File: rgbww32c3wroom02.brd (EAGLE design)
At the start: 36.8 x 20.3 mm, 25 parts

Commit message: small changes on the 12V side
moved the input caps so that the 12V pins are now oriented towards the switching controller. nothing major but might get a wee bit better filtering due to smaller loop area
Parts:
- moved C4 0.79 mm to (19.4, 77.6), turned to 90 degrees
- moved C3 0.16 mm to (22.1, 77.2), turned to 90 degrees
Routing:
- net 12V: track 11.6 -> 0.00 mm
- net GND: track 17.9 -> 17.2 mm
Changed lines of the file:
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@@
 <setting verticaltext="up"/>
 </settings>
-<grid distance="0.05" unitdist="inch" unit="inch" style="lines" multiple="1" display="no" altdistance="0.00625" altunitdist="inch" altunit="inch"/>
+<grid distance="0.05" unitdist="inch" unit="mm" style="lines" multiple="1" display="no" altdistance="0.00625" altunitdist="inch" altunit="mm"/>
 <layers>
 <layer number="1" name="Top" color="4" fill="1" visible="yes" active="yes"/>
@@
 Rev 23
 2023 Peter Jakobs</text>
+<text x="16.66875" y="72.86625" size="0.6096" layer="26" rot="MR90">ESP_RX</text>
 </plain>
 <attributes>
@@
 <element name="U$5" library="ESP32C3M" package="SMD" value="ESP32C3WROOM02" x="6.6675" y="69.85" rot="R90"/>
 <element name="U$6" library="TI_Components" package="SOT23-6" value="TPS5604030" x="20.32" y="70.485" rot="R180"/>
-<element name="C3" library="rcl" package="C1210" value="4.7µF" x="21.9075" y="77.1525" smashed="yes" rot="R270"/>
-<element name="C4" library="rcl" package="C0805" value="100nF" x="18.7325" y="77.1525" smashed="yes" rot="R270"/>
+<element name="C3" library="rcl" package="C1210" value="4.7µF" x="22.06625" y="77.1525" smashed="yes" rot="R90"/>
+<element name="C4" library="rcl" package="C0805" value="100nF" x="19.3675" y="77.62875" smashed="yes" rot="R90"/>
 <element name="R8" library="rcl" package="M0805" value="412kOhm" x="15.39875" y="77.31125" smashed="yes" rot="R90"/>
 <element name="R9" library="rcl" package="M0805" value="200kOhm" x="15.71625" y="77.31125" smashed="yes" rot="MR270">
@@
 <contactref element="C3" pad="2"/>
 <contactref element="C4" pad="2"/>
-<via x="18.7325" y="74.6125" extent="1-16" drill="0.6"/>
+<via x="17.4625" y="78.4225" extent="1-16" drill="0.6"/>
 <via x="22.225" y="71.755" extent="1-16" drill="0.6"/>
 <wire x1="20.57" y1="72.01" x2="21.97" y2="72.01" width="0.4064" layer="1"/>
 <wire x1="21.97" y1="72.01" x2="22.225" y2="71.755" width="0.4064" layer="1"/>
-<wire x1="18.7325" y1="74.6125" x2="18.7325" y2="76.2025" width="0.4064" layer="1"/>
-<wire x1="21.9075" y1="75.7525" x2="21.59" y2="74.93" width="0.4064" layer="1"/>
-<wire x1="21.59" y1="74.93" x2="21.2725" y2="74.6125" width="0.4064" layer="1"/>
-<wire x1="21.2725" y1="74.6125" x2="18.7325" y2="74.6125" width="0.4064" layer="1"/>
+<wire x1="17.4625" y1="78.4225" x2="19.21125" y2="78.4225" width="0.4064" layer="1"/>
+<wire x1="19.21125" y1="78.4225" x2="19.3675" y2="78.57875" width="0.4064" layer="1"/>
+<wire x1="19.3675" y1="78.57875" x2="22.04" y2="78.57875" width="0.4064" layer="1"/>
+<wire x1="22.04" y1="78.57875" x2="22.06625" y2="78.5525" width="0.4064" layer="1"/>
 </signal>
 <signal name="CH1">
@@
 <contactref element="SV1" pad="2"/>
 <polygon width="0.3048" layer="1">
-<vertex x="12.7" y="80.01"/>
+<vertex x="13.97" y="80.01"/>
 <vertex x="36.83" y="80.01"/>
 <vertex x="36.83" y="72.39"/>
@@
 <vertex x="23.1775" y="73.81875"/>
 <vertex x="23.1775" y="71.12"/>
-<vertex x="12.7" y="71.12"/>
+<vertex x="13.97" y="71.12"/>
 </polygon>
 <contactref element="U$6" pad="5"/>
@@
 <contactref element="C4" pad="1"/>
 <contactref element="C3" pad="1"/>
-<wire x1="22.0925" y1="78.42" x2="21.9075" y2="78.5525" width="0.4064" layer="1"/>
-<wire x1="18.32" y1="72.01" x2="19.305" y2="72.01" width="0.4064" layer="1"/>
-<wire x1="19.305" y1="72.01" x2="19.52625" y2="72.23125" width="0.4064" layer="1"/>
-<wire x1="19.52625" y1="72.23125" x2="19.52625" y2="73.50125" width="0.4064" layer="1"/>
-<wire x1="19.52625" y1="73.50125" x2="19.3675" y2="73.66" width="0.4064" layer="1"/>
-<wire x1="19.3675" y1="73.66" x2="17.30375" y2="73.66" width="0.4064" layer="1"/>
-<wire x1="17.30375" y1="73.66" x2="16.98625" y2="73.9775" width="0.4064" layer="1"/>
-<wire x1="16.98625" y1="73.9775" x2="16.98625" y2="78.105" width="0.4064" layer="1"/>
-<wire x1="16.98625" y1="78.105" x2="17.30375" y2="78.4225" width="0.4064" layer="1"/>
-<wire x1="17.30375" y1="78.4225" x2="18.25375" y2="78.4225" width="0.4064" layer="1"/>
-<wire x1="18.25375" y1="78.4225" x2="18.7325" y2="78.1025" width="0.4064" layer="1"/>
 </signal>
 <signal name="3V3">
@@
 <wire x1="12.7" y1="64.4525" x2="8.73125" y2="64.4525" width="0.3048" layer="1"/>
 <wire x1="23.1775" y1="63.97625" x2="23.1775" y2="65.0875" width="0.3048" layer="1"/>
-<wire x1="23.1775" y1="65.0875" x2="23.65375" y2="65.56375" width="0.3048" layer="1"/>
-<wire x1="23.65375" y1="65.56375" x2="24.60625" y2="65.56375" width="0.3048" layer="1"/>
-<wire x1="24.60625" y1="65.56375" x2="25.24125" y2="66.19875" width="0.3048" layer="1"/>
-<wire x1="25.24125" y1="66.19875" x2="25.24125" y2="67.0525" width="0.3048" layer="1"/>
+<wire x1="23.1775" y1="65.0875" x2="23.97125" y2="65.88125" width="0.3048" layer="1"/>
 <wire x1="25.24125" y1="67.0525" x2="25.34" y2="67.15125" width="0.3048" layer="1"/>
 <wire x1="13.6525" y1="63.5" x2="22.70125" y2="63.5" width="0.3048" layer="1"/>
 <wire x1="22.70125" y1="63.5" x2="23.1775" y2="63.97625" width="0.3048" layer="1"/>
+<wire x1="23.97125" y1="65.88125" x2="23.97125" y2="66.83375" width="0.3048" layer="1"/>
+<wire x1="25.24125" y1="67.0525" x2="24.19" y2="67.0525" width="0.3048" layer="1"/>
+<wire x1="24.19" y1="67.0525" x2="23.97125" y2="66.83375" width="0.3048" layer="1"/>
 </signal>
 <signal name="CH4S">

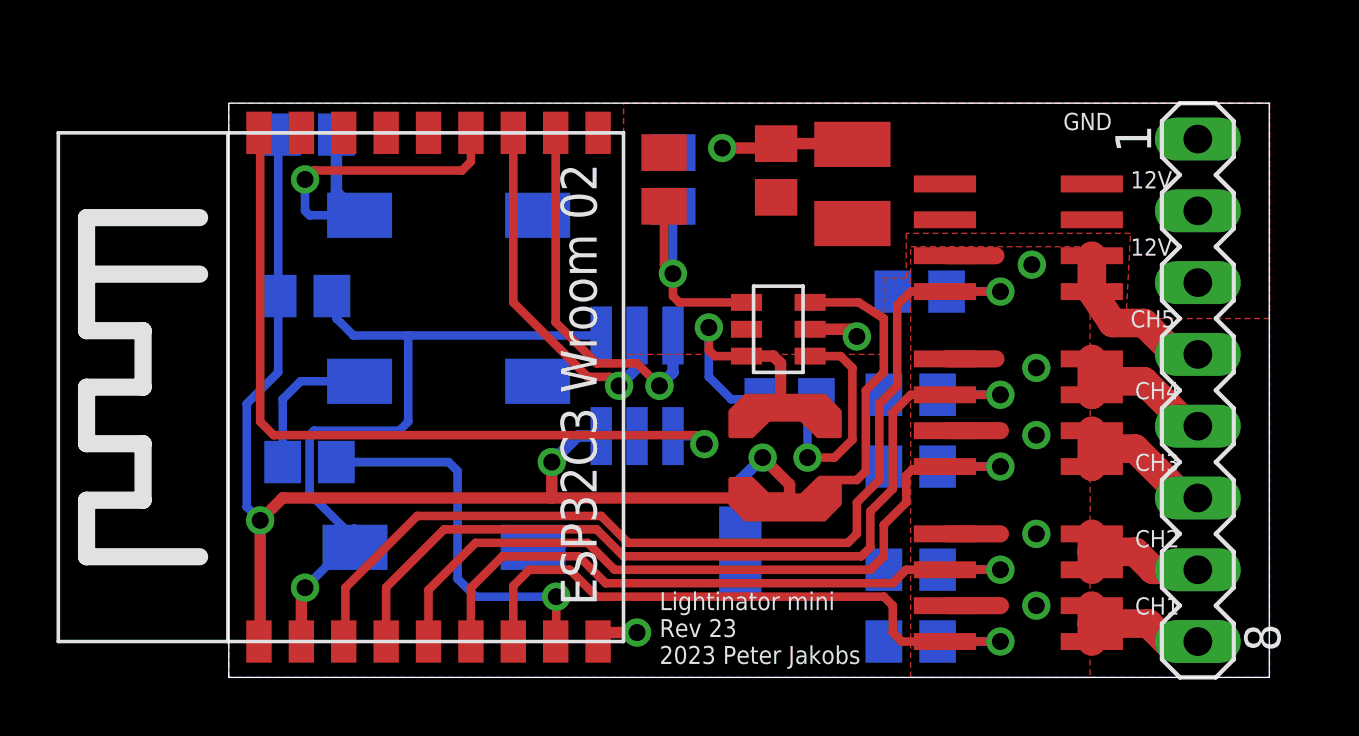
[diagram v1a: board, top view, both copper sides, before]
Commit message: corrected PRG pin for esp32c3
sometimes, I notice things way late. Like the fact that the PRG pin on the esp32c3 is no longer GPIO0 as it was with all xtensa based chips but now it's GPIO9.
I was using GPIO9 as an output pin with a 10k pulldown which should have always set the chip into download mode - not what I wanted. I have now shuffeled pins around and this should be ok now.
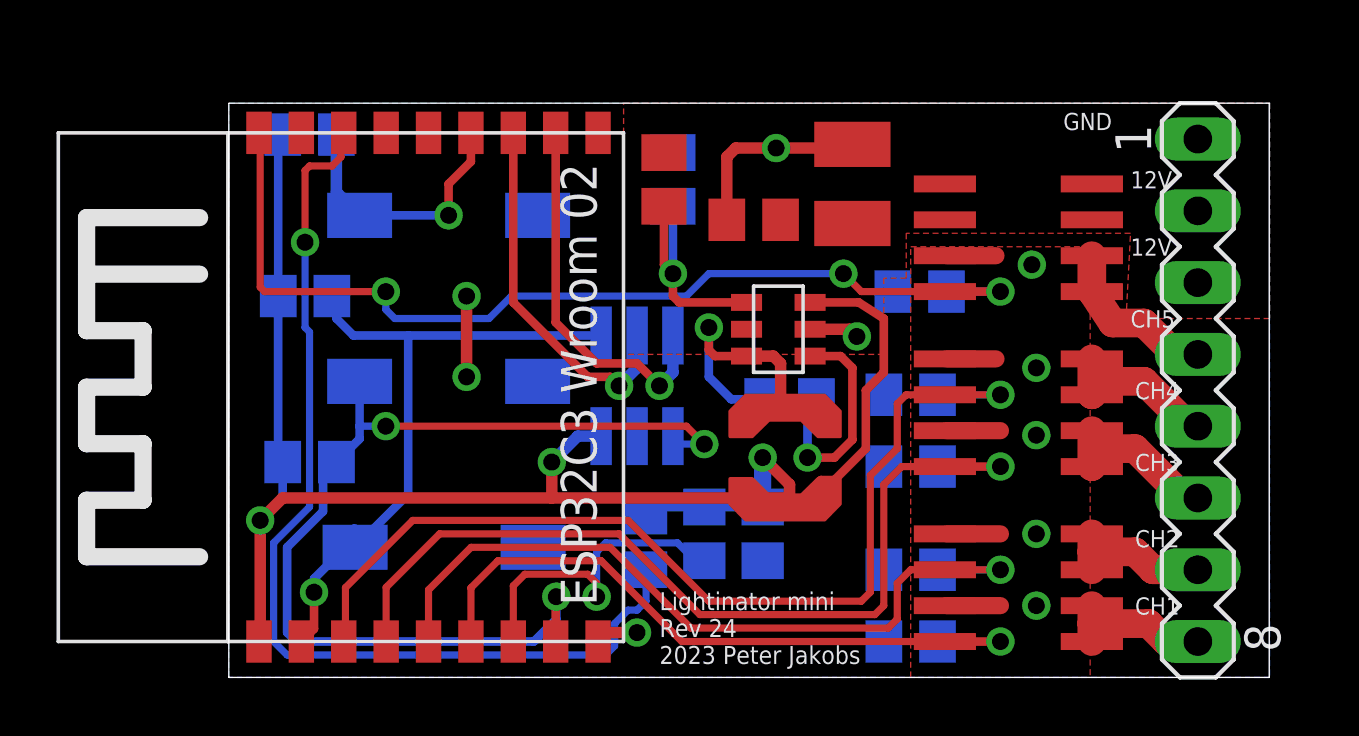
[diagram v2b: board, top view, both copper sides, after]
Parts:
- added R11, R12: 10k, rcl:R0805
- moved C4 1.92 mm to (18.6, 75.9), turned to 180 degrees
- moved C5 1.02 mm to (18.9, 64.8)
- turned R7 to 0 degrees
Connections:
- removed net CH1S: R4.1, U$1.4, U$5.P$3
- removed net CH2S: R3.1, U$1.2, U$5.P$4
- removed net CH3S: R2.1, U$2.4, U$5.P$5
- removed net CH4S: R5.1, U$2.2, U$5.P$6
- removed net CH5S: R1.2, U$3.4, U$5.P$7
- removed net GPIO0: J_PRG.6, U$5.P$18
- removed net N$5: U$5.P$16
- removed net PRG1: PRG.2, R7.1
- new net CH1A: R4.1, U$1.4, U$5.P$4
- new net CH2A: R3.1, U$1.2, U$5.P$5
- new net CH3A: R2.1, U$2.4, U$5.P$6
- new net CH4A: R5.1, U$2.2, U$5.P$7
- new net CH5A: R1.2, U$3.4, U$5.P$18
- new net IO2: R12.1, U$5.P$16
- new net IO8: R11.1, U$5.P$3
- net 3V3: now also R11.2, R12.2, R7.2
- net PRG: now also J_PRG.6, PRG.2, R7.1; no longer R7.2
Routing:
- net CH5S: track 36.0 -> 0.00 mm, vias 1 -> 0
- net CH4A: track 0.00 -> 35.9 mm, vias 0 -> 1
- net IO2: track 0.00 -> 35.4 mm, vias 0 -> 1
- net CH5A: track 0.00 -> 35.3 mm, vias 0 -> 3
- net CH4S: track 31.8 -> 0.00 mm, vias 1 -> 0
- net CH3A: track 0.00 -> 30.3 mm, vias 0 -> 1
- net CH3S: track 28.1 -> 0.00 mm, vias 1 -> 0
- net CH2A: track 0.00 -> 27.7 mm, vias 0 -> 1
- net GPIO0: track 27.6 -> 0.00 mm, vias 1 -> 0
- net CH2S: track 23.9 -> 0.00 mm, vias 1 -> 0
- net CH1S: track 23.3 -> 0.00 mm, vias 1 -> 0
- net PRG: track 13.6 -> 36.0 mm, vias 1 -> 3
- net CH1A: track 0.00 -> 22.2 mm, vias 0 -> 1
- net IO8: track 0.00 -> 11.2 mm, vias 0 -> 1
- net PRG1: track 5.21 -> 0.00 mm
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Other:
- board text added: "Lightinator mini Rev 24 2023 Peter Jakobs"
- board text removed: "Lightinator mini Rev 23 2023 Peter Jakobs"

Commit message: fixed a minor routing error
after viewing the result on aisler.net, I noticed that I had doubled up a via (the same via twice in the same location). Fixed that.
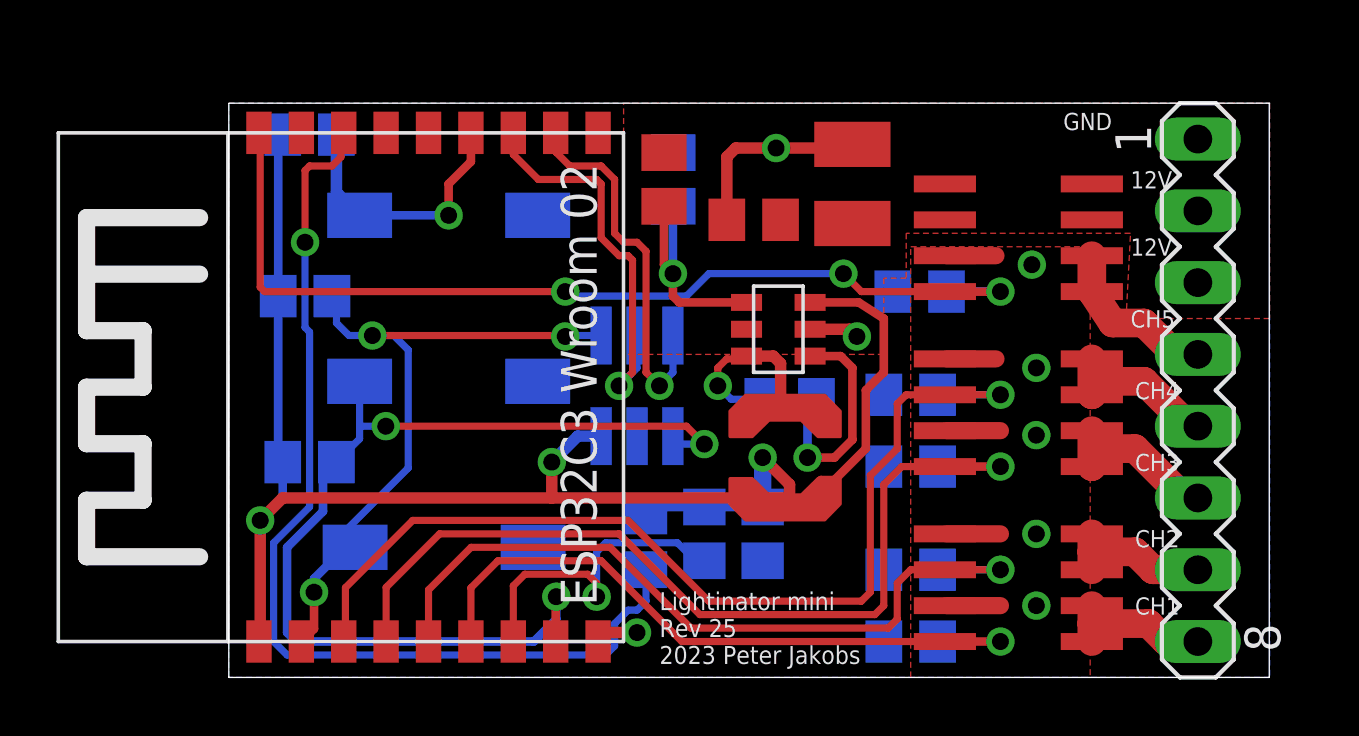
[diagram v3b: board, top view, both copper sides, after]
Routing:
- net GND: track 22.2 -> 19.4 mm, vias 10 -> 8
- net SW: track 9.01 -> 6.45 mm
- net TX: track 13.0 -> 14.3 mm
- net CH5A: track 35.3 -> 34.3 mm
- net EN: track 24.8 -> 25.5 mm, vias 1 -> 3
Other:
- board text added: "Lightinator mini Rev 25 2023 Peter Jakobs"
- board text removed: "Lightinator mini Rev 24 2023 Peter Jakobs"
